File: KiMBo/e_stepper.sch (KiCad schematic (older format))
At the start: 24 parts, among them U18 TMC2130

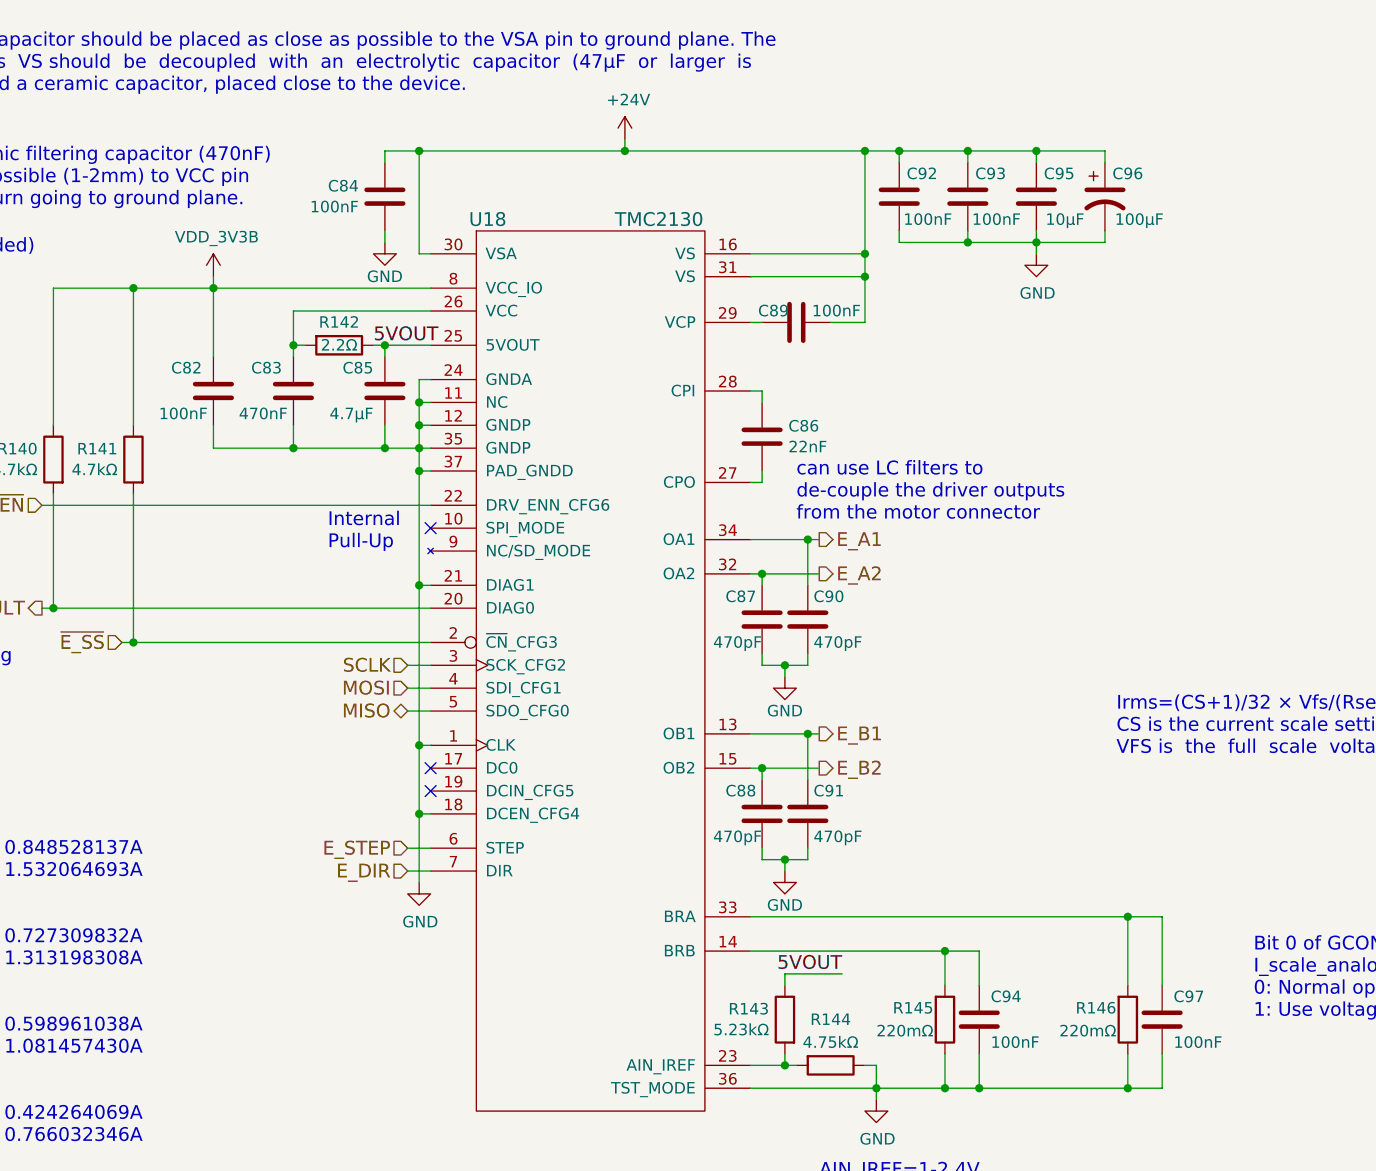
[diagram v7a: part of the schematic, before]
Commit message: Begin layout
Arrange all connectors to get a feel for the area.
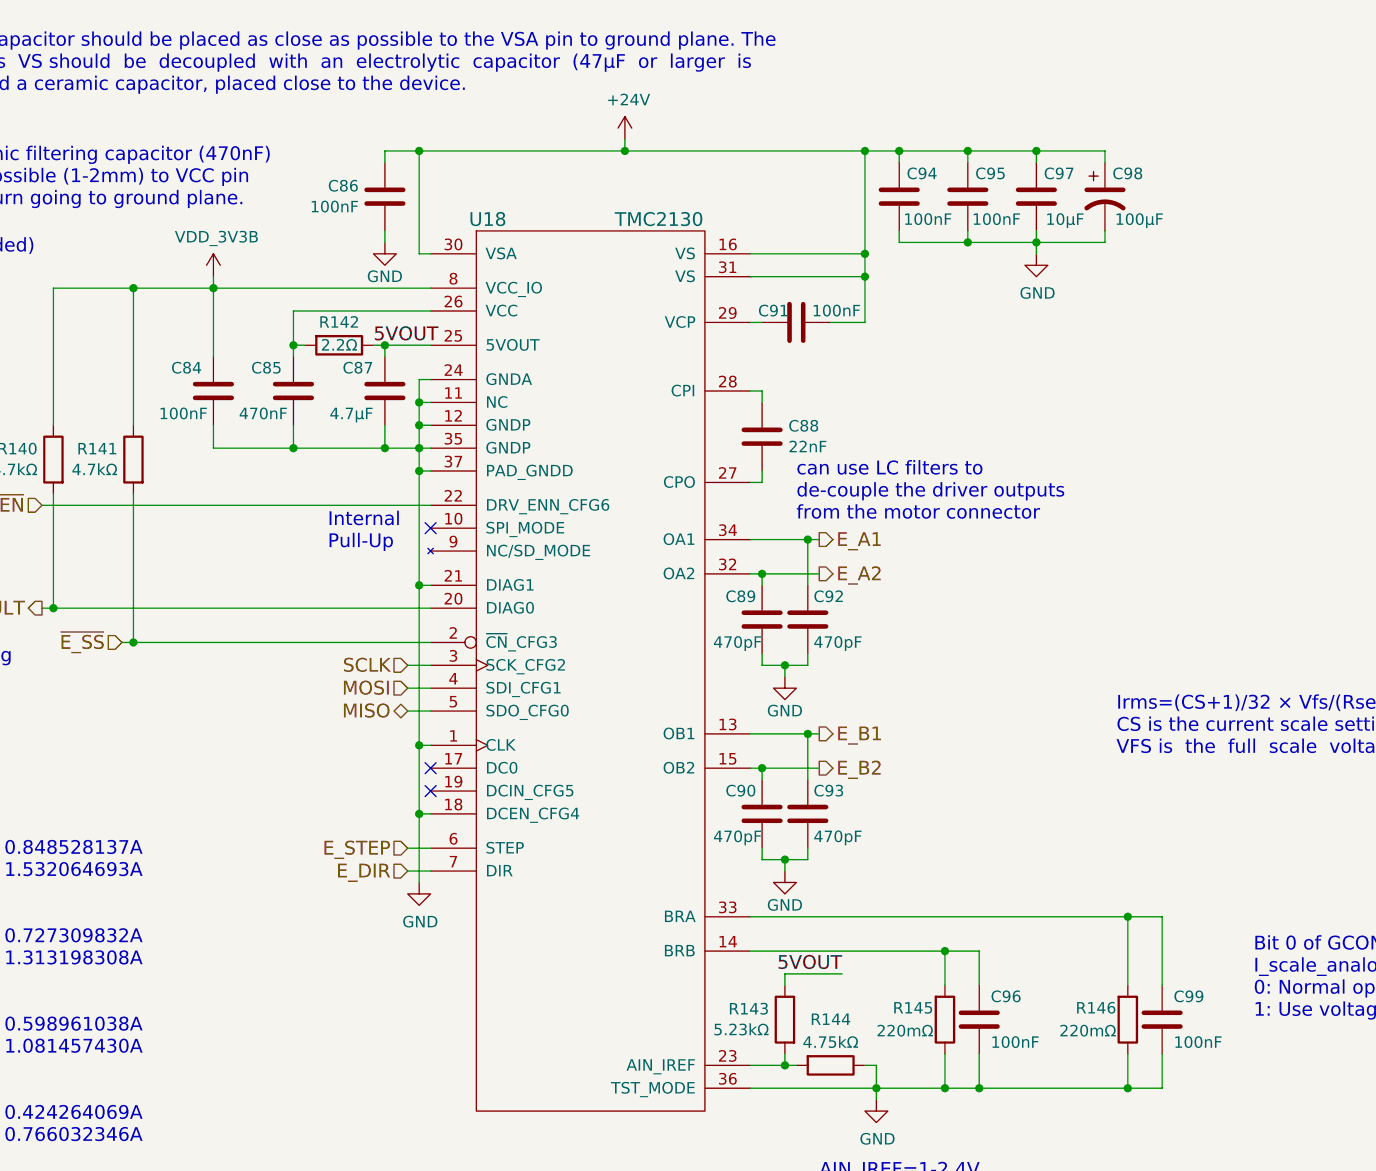
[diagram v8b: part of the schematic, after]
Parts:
- renumbered C82 to C84, C83 to C85, C84 to C86, C85 to C87, C86 to C88, C87 to C89, C88 to C90, C89 to C91, C90 to C92, C91 to C93, C92 to C94, C93 to C95, C94 to C96, C95 to C97, C96 to C98, C97 to C99
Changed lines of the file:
@@
 MOSI
 $Comp
-L C C84
+L C C86
 U 1 1 589B8A74
 P 7300 3950
-F 0 "C84" H 7186 3904 50  0000 R CNN
+F 0 "C86" H 7186 3904 50  0000 R CNN
 F 1 "100nF" H 7186 3995 50  0000 R CNN
 F 2 "Capacitors_SMD:C_0603" H 7338 3800 50  0001 C CNN
@@
 $EndComp
 $Comp
-L C C89
+L C C91
 U 1 1 5BA7E11F
 P 9100 4500
-F 0 "C89" V 9050 4400 50  0000 C CNN
+F 0 "C91" V 9050 4400 50  0000 C CNN
 F 1 "100nF" V 9050 4675 50  0000 C CNN
 F 2 "Capacitors_SMD:C_0603" H 9138 4350 50  0001 C CNN
@@
 $EndComp
 $Comp
-L CP1 C96
+L CP1 C98
 U 1 1 5BA7E120
 P 10450 3950
-F 0 "C96" H 10550 4050 50  0000 C CNN
+F 0 "C98" H 10550 4050 50  0000 C CNN
 F 1 "100μF" H 10600 3850 50  0000 C CNN
 F 2 "Capacitors_SMD:c_elec_8x10" H 10450 3950 50  0001 C CNN
@@
 $EndComp
 $Comp
-L C C92
+L C C94
 U 1 1 589BC941
 P 9550 3950
-F 0 "C92" H 9450 4050 50  0000 C CNN
+F 0 "C94" H 9450 4050 50  0000 C CNN
 F 1 "100nF" H 9425 3850 50  0000 C CNN
 F 2 "Capacitors_SMD:C_0603" H 9588 3800 50  0001 C CNN
@@
 $EndComp
 $Comp
-L GND #PWR0197
+L GND #PWR0200
 U 1 1 589BD203
 P 7300 4150
-F 0 "#PWR0197" H 7300 3900 50  0001 C CNN
+F 0 "#PWR0200" H 7300 3900 50  0001 C CNN
 F 1 "GND" H 7300 4000 50  0000 C CNN
 F 2 "" H 7300 4150 50  0000 C CNN
@@
 $EndComp
 $Comp
-L C C93
+L C C95
 U 1 1 589BDAA2
 P 9850 3950
-F 0 "C93" H 9750 4050 50  0000 C CNN
+F 0 "C95" H 9750 4050 50  0000 C CNN
 F 1 "100nF" H 9725 3850 50  0000 C CNN
 F 2 "Capacitors_SMD:C_0603" H 9888 3800 50  0001 C CNN
@@
 $EndComp
 $Comp
-L GND #PWR0198
+L GND #PWR0201
 U 1 1 589BE47E
 P 10150 4200
-F 0 "#PWR0198" H 10150 3950 50  0001 C CNN
+F 0 "#PWR0201" H 10150 3950 50  0001 C CNN
 F 1 "GND" H 10155 4027 50  0000 C CNN
 F 2 "" H 10150 4200 50  0000 C CNN
@@
 $EndComp
 $Comp
-L +24V #PWR0199
+L +24V #PWR0202
 U 1 1 5BA7E125
 P 8350 3700
-F 0 "#PWR0199" H 8350 3550 50  0001 C CNN
+F 0 "#PWR0202" H 8350 3550 50  0001 C CNN
 F 1 "+24V" H 8365 3873 50  0000 C CNN
 F 2 "" H 8350 3700 50  0000 C CNN
@@
 $EndComp
 $Comp
-L C C86
+L C C88
 U 1 1 589C0BAD
 P 8950 5000
-F 0 "C86" H 9065 5046 50  0000 L CNN
+F 0 "C88" H 9065 5046 50  0000 L CNN
 F 1 "22nF" H 9065 4955 50  0000 L CNN
 F 2 "Capacitors_SMD:C_0603" H 8988 4850 50  0001 C CNN
@@
 $EndComp
 $Comp
-L GND #PWR0200
+L GND #PWR0203
 U 1 1 5BA7E129
 P 9450 7900
-F 0 "#PWR0200" H 9450 7650 50  0001 C CNN
+F 0 "#PWR0203" H 9450 7650 50  0001 C CNN
 F 1 "GND" H 9455 7727 50  0000 C CNN
 F 2 "" H 9450 7900 50  0000 C CNN
@@
 $EndComp
 $Comp
-L C C83
+L C C85
 U 1 1 589C52DF
 P 6900 4800
-F 0 "C83" H 6950 4900 50  0000 L CNN
+F 0 "C85" H 6950 4900 50  0000 L CNN
 F 1 "470nF" H 6925 4700 50  0000 L CNN
 F 2 "Capacitors_SMD:C_0603" H 6938 4650 50  0001 C CNN
@@
 NoConn ~ 7500 6550
 $Comp
-L GND #PWR0201
+L GND #PWR0204
 U 1 1 589C97FF
 P 7450 6950
-F 0 "#PWR0201" H 7450 6700 50  0001 C CNN
+F 0 "#PWR0204" H 7450 6700 50  0001 C CNN
 F 1 "GND" H 7455 6777 50  0000 C CNN
 F 2 "" H 7450 6950 50  0000 C CNN
@@
 $EndComp
 $Comp
-L C C94
+L C C96
 U 1 1 5BA7E12E
 P 9900 7550
-F 0 "C94" H 9950 7650 50  0000 L CNN
+F 0 "C96" H 9950 7650 50  0000 L CNN
 F 1 "100nF" H 9950 7450 50  0000 L CNN
 F 2 "Capacitors_SMD:C_0603" H 9938 7400 50  0001 C CNN
@@
 Internal\nPull-Up
 $Comp
-L C C85
+L C C87
 U 1 1 5BA7E12A
 P 7300 4800
-F 0 "C85" H 7350 4900 50  0000 L CNN
+F 0 "C87" H 7350 4900 50  0000 L CNN
 F 1 "4.7μF" H 7350 4700 50  0000 L CNN
 F 2 "Capacitors_SMD:C_0603" H 7338 4650 50  0001 C CNN
@@
 $EndComp
 $Comp
-L C C97
+L C C99
 U 1 1 5BA7E133
 P 10700 7550
-F 0 "C97" H 10750 7650 50  0000 L CNN
+F 0 "C99" H 10750 7650 50  0000 L CNN
 F 1 "100nF" H 10750 7450 50  0000 L CNN
 F 2 "Capacitors_SMD:C_0603" H 10738 7400 50  0001 C CNN
@@
 Choose  sense  resistors  in  a  way,  that  normal \nIRUN is 16 to 31 for best microstep performance.
 $Comp
-L C C87
+L C C89
 U 1 1 5BA7E134
 P 8950 5800
-F 0 "C87" H 8975 5900 50  0000 L CNN
+F 0 "C89" H 8975 5900 50  0000 L CNN
 F 1 "470pF" H 8950 5700 50  0000 L CNN
 F 2 "Capacitors_SMD:C_0603" H 8988 5650 50  0001 C CNN
@@
 $EndComp
 $Comp
-L GND #PWR0202
+L GND #PWR0205
 U 1 1 58B19D33
 P 9050 6050
-F 0 "#PWR0202" H 9050 5800 50  0001 C CNN
+F 0 "#PWR0205" H 9050 5800 50  0001 C CNN
 F 1 "GND" H 9050 5900 50  0000 C CNN
 F 2 "" H 9050 6050 50  0000 C CNN
@@
 $EndComp
 $Comp
-L C C90
+L C C92
 U 1 1 58B1B794
 P 9150 5800
-F 0 "C90" H 9175 5900 50  0000 L CNN
+F 0 "C92" H 9175 5900 50  0000 L CNN
 F 1 "470pF" H 9175 5700 50  0000 L CNN
 F 2 "Capacitors_SMD:C_0603" H 9188 5650 50  0001 C CNN
@@
 $EndComp
 $Comp
-L C C88
+L C C90
 U 1 1 58B1C6FD
 P 8950 6650
-F 0 "C88" H 8975 6750 50  0000 L CNN
+F 0 "C90" H 8975 6750 50  0000 L CNN
 F 1 "470pF" H 8950 6550 50  0000 L CNN
 F 2 "Capacitors_SMD:C_0603" H 8988 6500 50  0001 C CNN
@@
 $EndComp
 $Comp
-L GND #PWR0203
+L GND #PWR0206
 U 1 1 58B1C704
 P 9050 6900
-F 0 "#PWR0203" H 9050 6650 50  0001 C CNN
+F 0 "#PWR0206" H 9050 6650 50  0001 C CNN
 F 1 "GND" H 9050 6750 50  0000 C CNN
 F 2 "" H 9050 6900 50  0000 C CNN
@@
 $EndComp
 $Comp
-L C C91
+L C C93
 U 1 1 58B1C710
 P 9150 6650
-F 0 "C91" H 9175 6750 50  0000 L CNN
+F 0 "C93" H 9175 6750 50  0000 L CNN
 F 1 "470pF" H 9175 6550 50  0000 L CNN
 F 2 "Capacitors_SMD:C_0603" H 9188 6500 50  0001 C CNN
@@
 $EndComp
 $Comp
-L C C95
+L C C97
 U 1 1 58B40194
 P 10150 3950
-F 0 "C95" H 10050 4050 50  0000 C CNN
+F 0 "C97" H 10050 4050 50  0000 C CNN
 F 1 "10μF" H 10025 3850 50  0000 C CNN
 F 2 "Capacitors_SMD:C_0805" H 10188 3800 50  0001 C CNN
@@
 Can extract which\nfault is occurring via SPI\nby reading DRV_STATUS reg
 $Comp
-L VDD_3V3B #PWR0204
+L VDD_3V3B #PWR0207
 U 1 1 5A2FD350
 P 6550 4300
-F 0 "#PWR0204" H 6550 4150 50  0001 C CNN
+F 0 "#PWR0207" H 6550 4150 50  0001 C CNN
 F 1 "VDD_3V3B" H 6565 4473 50  0000 C CNN
 F 2 "" H 6550 4300 50  0000 C CNN
@@
 $EndComp
 $Comp
-L C C82
+L C C84
 U 1 1 5A896678
 P 6550 4800
-F 0 "C82" H 6600 4900 50  0000 L CNN
+F 0 "C84" H 6600 4900 50  0000 L CNN
 F 1 "100nF" H 6575 4700 50  0000 L CNN
 F 2 "Capacitors_SMD:C_0603" H 6588 4650 50  0001 C CNN
